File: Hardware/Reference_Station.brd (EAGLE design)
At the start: 166.1 x 131.1 mm, 399 parts, among them J10 ANTENNA-SMA-GROUNDEDEDGE_SMA, J11 Vertical Qwiic Connector, J2 ANTENNA-SMA-GROUNDEDEDGE_SMA, J3 MICRO-SD-PUSH-PUSH-EXT-PIN, J4 Vertical Qwiic Connector, J7 ANTENNA-SMA-GROUNDEDEDGE_RPSMA, J9 MAGJACK-POE, U1 ESP-WROOM-32E, U10 POE_PSU-DP990X, U11 OPA344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

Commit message: v10 Hardware
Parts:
- removed E$1, E$2, E$3, E$4: (no value), SparkFun-Aesthetics:FIDUCIAL-1X2
- removed E$5, E$6: (no value), SparkFun-Retired:FIDUCIAL-1.5X3
- added C58: 0.1uF, SparkFun-Capacitors:0603
- added DET: TEST-POINTPOGO_PTH, SparkFun-Connectors:1X01_NO_SILK
- added FRAME1: FRAME-LEDGER, SparkFun-Aesthetics:CREATIVE_COMMONS
- added GNSS_RESET: JUMPER-COMBO_2_NO, SparkFun-Jumpers:COMBO-JUMPER_2_NO
- added LOGO1: SPECIAL_INSTRUCTIONS-ORDERING, SparkFun-Aesthetics:ORDERING_INSTRUCTIONS
- added R64: 10k, SparkFun-Resistors:0603
- added R65: 100k, SparkFun-Resistors:0603
- added U$154: (no value), output:#GNSS_RESET#0
- added U$155, U$156: (no value), output:DET0
- C31: value DNP -> 0.1uF; device SparkFun-Capacitors:0603_NO_CREAM -> SparkFun-Capacitors:0603
- U$70: device output:CORS_AND_TIME0 -> output:#GNSS_#RESET##0
- U$74: device output:CORS_AND_TIME0 -> output:#RESET#0
- U8: value ADC8045 -> MCP6021T; device SparkFun-IC-Amplifiers:SO08_PAD -> SparkFun-IC-Amplifiers:SOT23-5
- U9: value 74HC4066_QUAD_BILATERAL_SWITCH_QFN -> 74LVC4066D_QUAD_BILATERAL_SWITCH; device SparkFun-IC-Logic:14-QFN -> SparkFun-IC-Logic:SO14
- moved U$74 48.6 mm to (113.0, 61.0), flipped to the top
- moved U$70 35.5 mm to (118.1, 62.9), flipped to the bottom
- moved C23 10.2 mm to (120.7, 86.7), turned to 270 degrees
- moved U$22 10.2 mm to (112.4, 99.4)
- moved U$21 10.2 mm to (90.2, 101.1)
- moved C22 9.26 mm to (120.7, 91.1), turned to 90 degrees
- moved U$41 5.54 mm to (147.8, 61.0)
- moved C26 3.25 mm to (37.5, 32.4)
- moved U9 2.87 mm to (35.6, 26.7), turned to 270 degrees
- moved R23 2.57 mm to (116.0, 85.1), turned to 0 degrees
- moved R18 2.57 mm to (117.2, 82.5)
- moved R44 2.57 mm to (114.7, 82.5)
- moved U$71 2.57 mm to (116.0, 83.4)
- moved V_TP 2.57 mm to (116.0, 82.5)
- moved U$152 2.54 mm to (129.5, 22.9)
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- renumbered VPOE7 to GND
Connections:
- removed net N$16: R9.2, U8.6
- new net DET: DET.1, J3.9, R65.1, U1.4
- new net GNSS_!RESET!: C58.1, GNSS_RESET.1, GNSS_RESET.3, R64.1, U4.49
- net !RESET!: now also GNSS_RESET.2, GNSS_RESET.4; no longer U4.49
- net 3.3V: now also R64.2
- net 3.3V_SW: now also R65.2
- net 5V: now also U8.5; no longer U8.7
- net GND: now also C58.2, U8.2; no longer U8.4, U8.PAD, U9.EPAD
- net N$18: now also U8.4; no longer U8.2
- net N$26: now also R9.2
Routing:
- net DET: track 0.00 -> 118.1 mm, vias 0 -> 4
- net GNSS_!RESET!: track 0.00 -> 35.8 mm, vias 0 -> 1
- net !RESET!: track 256.6 -> 226.9 mm, vias 9 -> 8
- net ESP25/TP: track 101.6 -> 113.9 mm
- net N$26: track 7.10 -> 13.9 mm, vias 1 -> 2
- net 5V: track 225.2 -> 219.4 mm, vias 43 -> 45
- net ESP2/DAT0: track 89.6 -> 94.2 mm
- net SD_CMD: track 17.4 -> 21.2 mm
- net SD_DAT2: track 23.4 -> 27.0 mm
- net PWREN: track 89.6 -> 93.1 mm, vias 4 -> 2
- net 3.3V_SW: track 348.0 -> 351.3 mm
- net N$16: track 2.96 -> 0.00 mm
- net ESP15/CMD: track 88.8 -> 91.3 mm
- net SD_DAT0: track 25.5 -> 27.8 mm
- net N$29: track 3.71 -> 5.49 mm
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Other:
- board size 166.1 x 131.1 mm -> 151.8 x 101.6 mm
- board text added: "4-Layers 1.6mm Thickness 1oz Copper Lead-Free HASL Finish Red Solder Resist White Silkscreen"
- board text added: "Dimensions In Inches"
- board text added: "Paul Clark"
- board text added: "V-Score To V-Score"
- board text added: "v10"
- board text removed: "Route Out"
- board text removed: "v-score"
- board text removed: "v01"

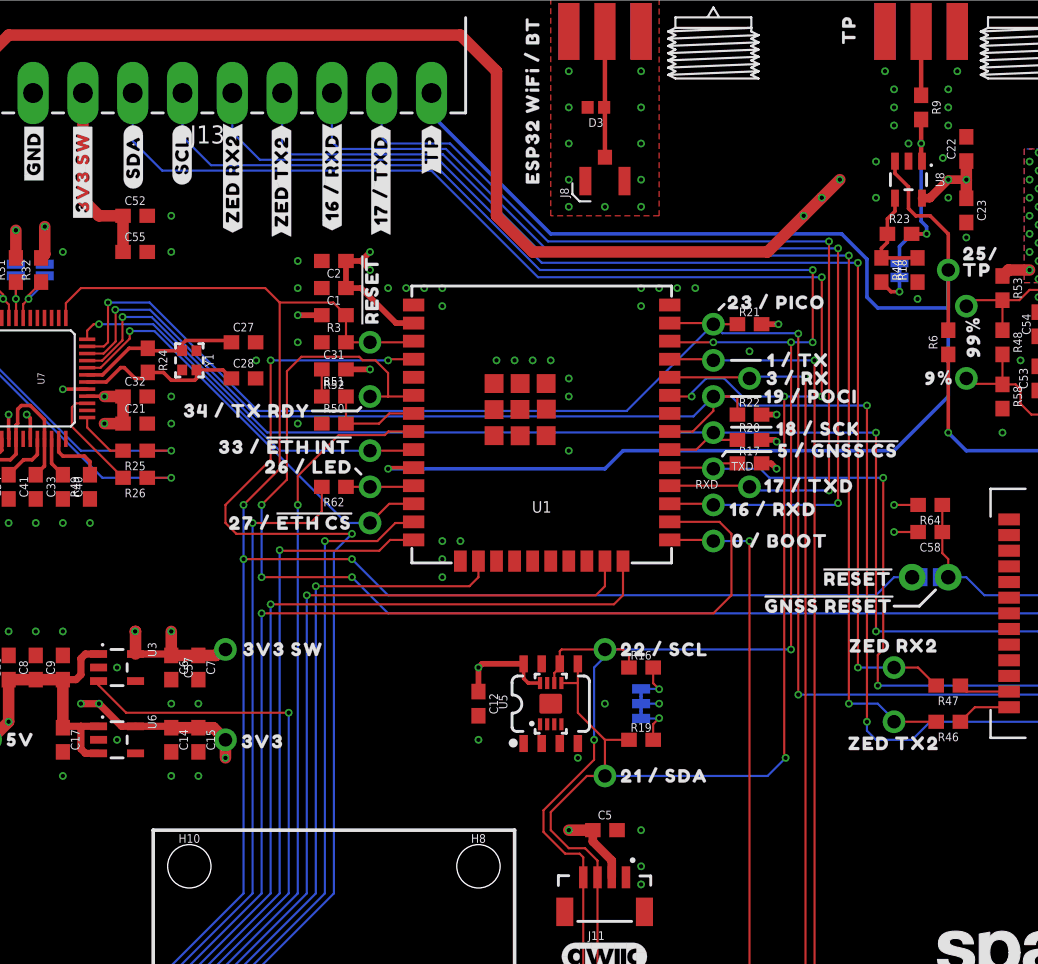
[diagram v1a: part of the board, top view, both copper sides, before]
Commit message: Improve TP output at 5V
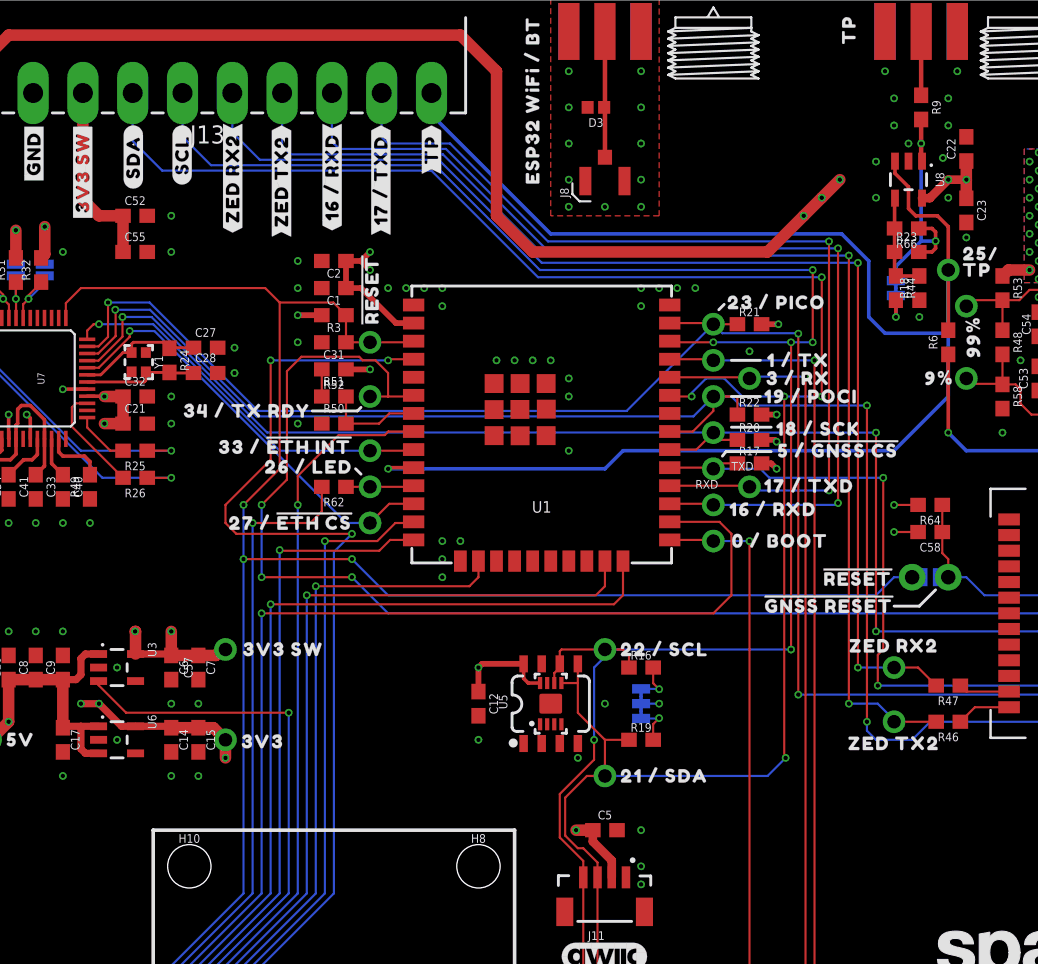
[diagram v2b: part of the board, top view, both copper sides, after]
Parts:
- added R66: 100k, SparkFun-Resistors:0603
- moved Y1 3.56 mm to (62.5, 76.1)
- moved C27 2.69 mm to (67.2, 77.1)
- moved C28 2.69 mm to (67.2, 75.3)
- moved R44 1.63 mm to (115.7, 81.3)
- moved R24 1.52 mm to (64.6, 76.2)
- moved R23 1.37 mm to (116.5, 83.8)
- moved U$71 1.30 mm to (115.7, 82.2)
- moved V_TP 1.30 mm to (115.7, 81.3)
- moved R18 1.28 mm to (117.3, 81.3)
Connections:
- net N$18: now also R66.2
- net N$26: now also R66.1
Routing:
- net N$26: track 13.9 -> 18.1 mm
- net N$20: track 12.2 -> 8.16 mm
- net ESP25/TP: track 113.9 -> 117.5 mm
- net N$19: track 11.6 -> 8.96 mm
- net ESP22/SCL: track 171.6 -> 170.0 mm
- net ESP21/SDA: track 180.3 -> 179.0 mm
- net GND: vias 327 -> 326

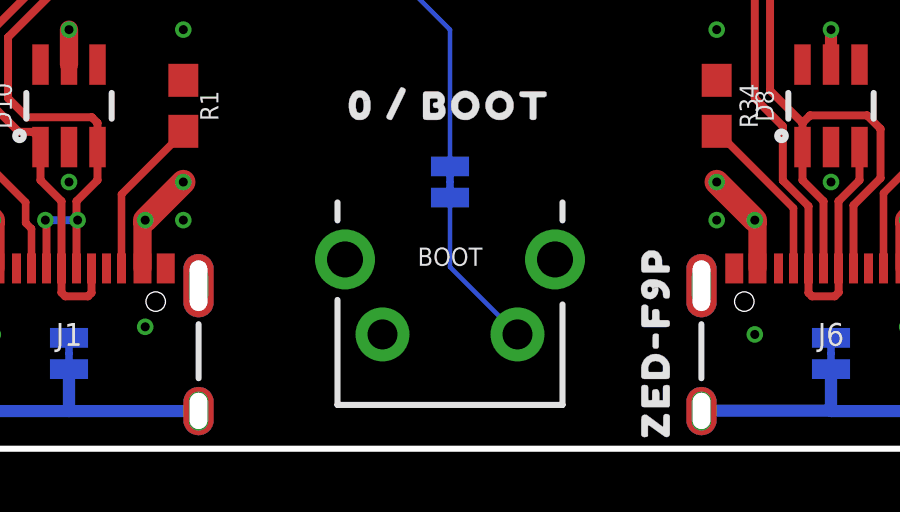
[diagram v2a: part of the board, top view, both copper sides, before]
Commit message: Move BOOT / MODE button further out. Update panels and stickers
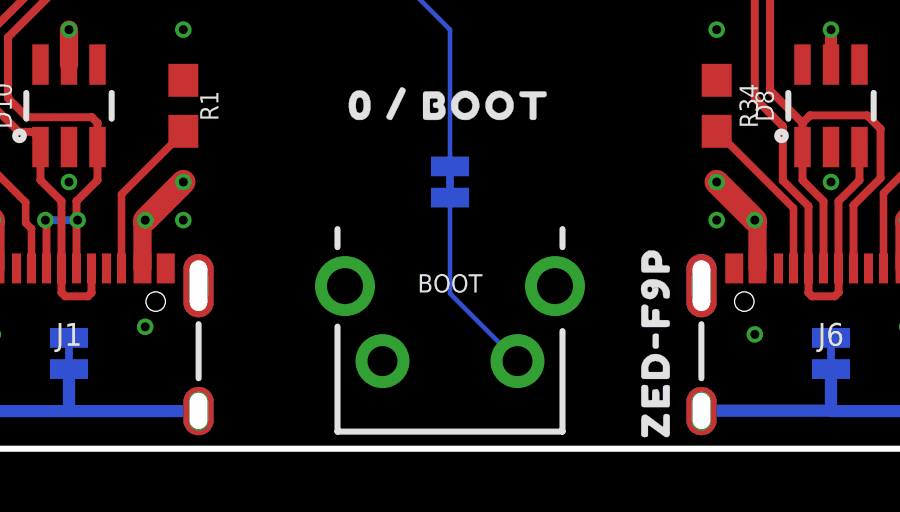
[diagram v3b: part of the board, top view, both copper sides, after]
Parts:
- moved BOOT 0.89 mm to (127.0, 2.92)
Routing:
- net N$29: track 5.49 -> 6.38 mm
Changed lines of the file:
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@@
 <attribute name="PROD_ID" value="SWCH-13896" x="101.6" y="3.81" size="1.778" layer="27" ratio="15" display="off"/>
 </element>
-<element name="BOOT" library="SparkFun-Switches" package="TACTILE_SWITCH_PTH_RA_8-020" value="MOMENTARY-SWITCH-SPST-PTH-RIGHT-ANGLE-8-020" x="127" y="3.81" smashed="yes">
-<attribute name="NAME" x="127" y="6.096" size="0.6096" layer="25" font="vector" ratio="20" align="bottom-center"/>
-<attribute name="PROD_ID" value="SWCH-13896" x="127" y="3.81" size="1.778" layer="27" ratio="15" display="off"/>
+<element name="BOOT" library="SparkFun-Switches" package="TACTILE_SWITCH_PTH_RA_8-020" value="MOMENTARY-SWITCH-SPST-PTH-RIGHT-ANGLE-8-020" x="127" y="2.921" smashed="yes">
+<attribute name="NAME" x="127" y="5.207" size="0.6096" layer="25" font="vector" ratio="20" align="bottom-center"/>
+<attribute name="PROD_ID" value="SWCH-13896" x="127" y="2.921" size="1.778" layer="27" ratio="15" display="off"/>
 </element>
 <element name="LED" library="SparkFun-Jumpers" package="SMT-JUMPER_2_NC_TRACE_SILK" package3d_urn="urn:adsk.eagle:package:39281/1" value="JUMPER-SMT_2_NC_TRACE_SILK" x="12.7" y="3.175" smashed="yes" rot="MR180">
@@
 <contactref element="BOOT" pad="2"/>
 <contactref element="BOOT_SW" pad="2"/>
-<wire x1="129.25" y1="3.81" x2="127" y2="6.06" width="0.1524" layer="16"/>
-<wire x1="127" y1="6.06" x2="127" y2="8.3693" width="0.1524" layer="16"/>
+<wire x1="127" y1="5.171" x2="129.25" y2="2.921" width="0.1524" layer="16"/>
+<wire x1="127" y1="8.3693" x2="127" y2="5.171" width="0.1524" layer="16"/>
 </signal>
 <signal name="GNSS_!RESET!">

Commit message: Replace OPA344 with MCP6021T-E/OT
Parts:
- U11, U13: value OPA344 -> MCP6021T
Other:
- board text added: "JLCPCB JLC-7628 Impedance Control 4-Layers Thickness: 1.6mm Outer Copper: 1oz Finish: HASL Lead Free Red Solder Resist White Silkscreen"
- board text removed: "4-Layers 1.6mm Thickness 1oz Copper Lead-Free HASL Finish Red Solder Resist White Silkscreen"
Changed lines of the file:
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@@
 <dimension x1="0" y1="101.6" x2="0" y2="0" x3="-8.89" y3="50.8" textsize="1.778" textratio="15" layer="47" dtype="vertical" unit="inch"/>
 <text x="213.36" y="0" size="1.778" layer="51" font="vector" ratio="15">Paul Clark</text>
-<text x="160.02" y="49.53" size="1.778" layer="51" font="vector" ratio="15" align="top-left">4-Layers
-1.6mm Thickness
-1oz Copper
-Lead-Free HASL Finish
+<text x="160.02" y="49.53" size="1.778" layer="51" font="vector" ratio="15" align="top-left">JLCPCB JLC-7628 Impedance Control
+4-Layers
+Thickness: 1.6mm
+Outer Copper: 1oz
+Finish: HASL Lead Free
 Red Solder Resist
 White Silkscreen
@@
 <attribute name="VALUE" x="119.38" y="54.102" size="0.6096" layer="27" font="vector" ratio="20" rot="R180" align="top-center"/>
 </element>
-<element name="U11" library="SparkFun-IC-Amplifiers" package="SOT23-5" value="OPA344" x="128.905" y="78.74" smashed="yes" rot="R90">
+<element name="U11" library="SparkFun-IC-Amplifiers" package="SOT23-5" value="MCP6021T" x="128.905" y="78.74" smashed="yes" rot="R90">
 <attribute name="NAME" x="128.905" y="76.835" size="0.6096" layer="25" font="vector" ratio="20" rot="R180" align="bottom-center"/>
-<attribute name="PROD_ID" value="IC-08251" x="125.095" y="74.93" size="1.778" layer="27" ratio="15" rot="R90" display="off"/>
-<attribute name="VALUE" x="128.905" y="81.28" size="0.6096" layer="27" font="vector" ratio="20" rot="R180" align="bottom-center"/>
+<attribute name="PROD_ID" value="IC-12504" x="125.095" y="74.93" size="1.778" layer="27" ratio="15" rot="R90" display="off"/>
+<attribute name="VALUE" value="MCP6021T" x="128.905" y="81.28" size="0.6096" layer="27" font="vector" ratio="20" rot="R180" align="bottom-center"/>
 </element>
 <element name="C54" library="SparkFun-Capacitors" package="0603" value="0.1uF" x="125.73" y="78.74" smashed="yes" rot="R90">
@@
 <attribute name="VALUE" x="133.477" y="78.74" size="0.6096" layer="27" font="vector" ratio="20" rot="R90" align="top-center"/>
 </element>
-<element name="U13" library="SparkFun-IC-Amplifiers" package="SOT23-5" value="OPA344" x="128.905" y="74.93" smashed="yes" rot="R90">
+<element name="U13" library="SparkFun-IC-Amplifiers" package="SOT23-5" value="MCP6021T" x="128.905" y="74.93" smashed="yes" rot="R90">
 <attribute name="NAME" x="128.905" y="73.025" size="0.6096" layer="25" font="vector" ratio="20" rot="R180" align="bottom-center"/>
-<attribute name="PROD_ID" value="IC-08251" x="128.905" y="74.93" size="1.778" layer="27" ratio="15" rot="R90" display="off"/>
-<attribute name="VALUE" x="128.905" y="77.47" size="0.6096" layer="27" font="vector" ratio="20" rot="R180" align="bottom-center"/>
+<attribute name="PROD_ID" value="IC-12504" x="128.905" y="74.93" size="1.778" layer="27" ratio="15" rot="R90" display="off"/>
+<attribute name="VALUE" value="MCP6021T" x="128.905" y="77.47" size="0.6096" layer="27" font="vector" ratio="20" rot="R180" align="bottom-center"/>
 </element>
 <element name="R57" library="SparkFun-Resistors" package="0603" value="10k" x="134.62" y="71.12" smashed="yes" rot="R270">

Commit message: Change LED to GREEN
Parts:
- D2: value LED-RIGHT-ANGLE-PTH-BLUE -> LED-RIGHT-ANGLE-PTH-GREEN
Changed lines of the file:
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@@
 <attribute name="NAME" x="12.7" y="2.032" size="0.6096" layer="26" font="vector" ratio="20" rot="MR180" align="bottom-center"/>
 </element>
-<element name="D2" library="SparkFun-LED" package="CBI-RIGHT-ANGLE-PTH" value="LED-RIGHT-ANGLE-PTH-BLUE" x="12.7" y="0.635" smashed="yes">
+<element name="D2" library="SparkFun-LED" package="CBI-RIGHT-ANGLE-PTH" value="LED-RIGHT-ANGLE-PTH-GREEN" x="12.7" y="0.635" smashed="yes">
 <attribute name="NAME" x="12.7" y="10.795" size="1.27" layer="25" font="vector" rot="SR0" align="bottom-center"/>
-<attribute name="PROD_ID" value="DIO-13890" x="12.7" y="0.635" size="1.778" layer="27" ratio="15" display="off"/>
+<attribute name="PROD_ID" value="DIO-13847" x="12.7" y="0.635" size="1.778" layer="27" ratio="15" display="off"/>
 </element>
 <element name="R62" library="SparkFun-Resistors" package="0603" value="470" x="76.2" y="67.31" smashed="yes" rot="R180">
